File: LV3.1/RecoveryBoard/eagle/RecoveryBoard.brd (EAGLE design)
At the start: 120.9 x 54.6 mm, 92 parts, among them IC1 BD62120AEFJ-E2, Q1 BSS123, Q2 BSS123, Q3 BSS123, Q6 MOSFET-PCH-SOT23-6, U1 STM32F042K6, U10 TPS63070, Y1 ECS-160-10-36Q-ES-TR

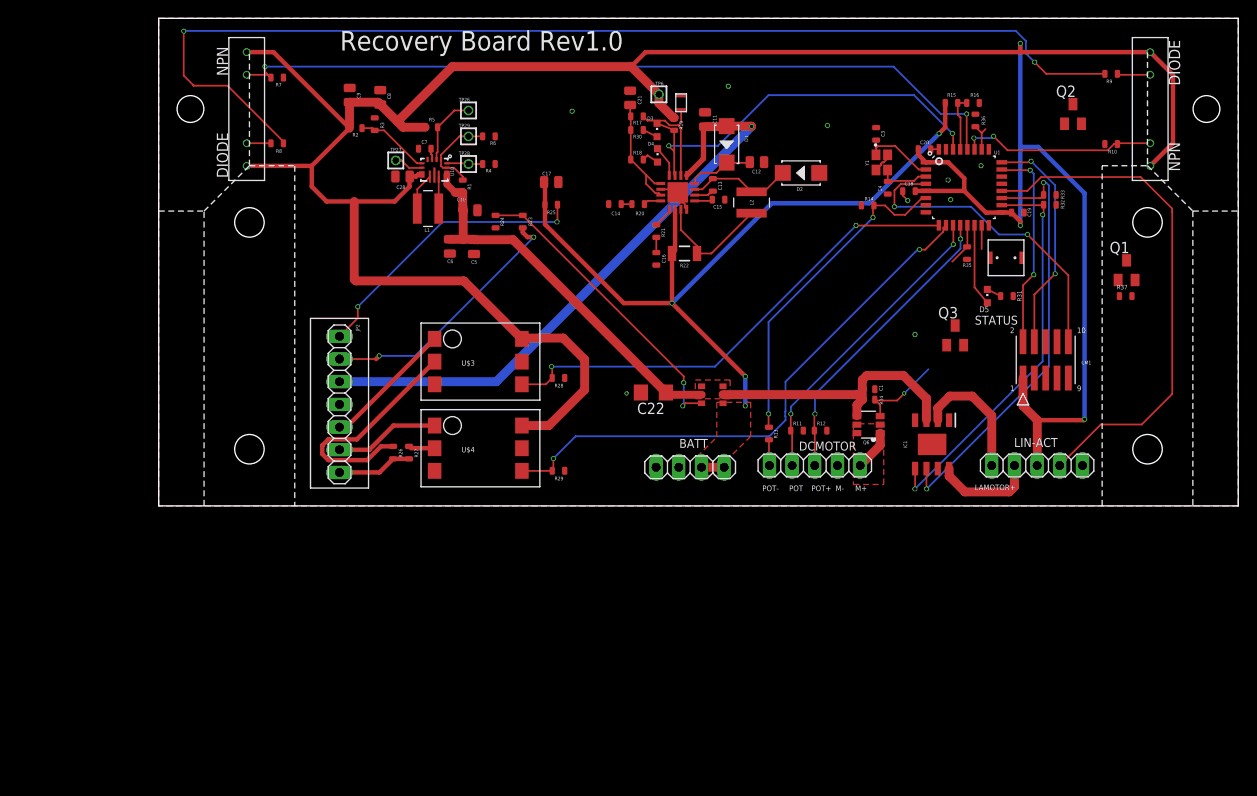
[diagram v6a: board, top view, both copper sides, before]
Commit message: edited board after design meeting on 1/15
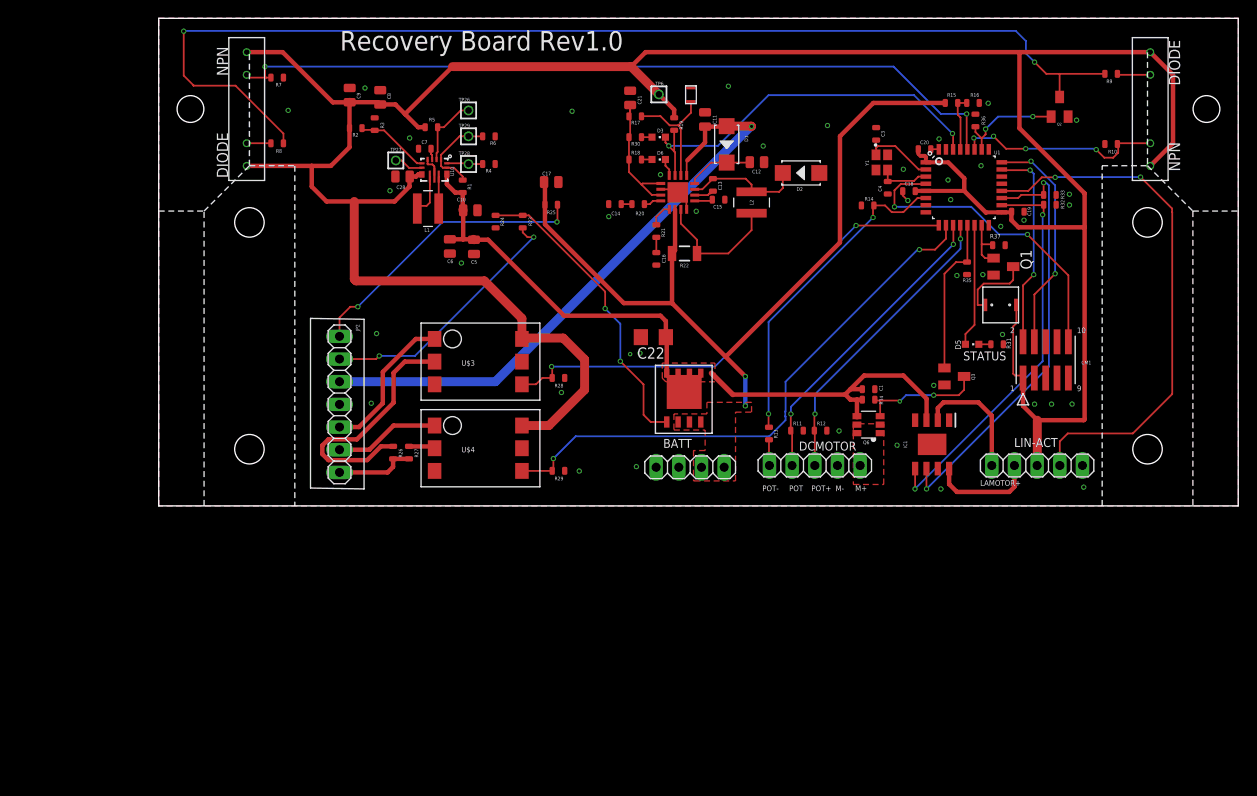
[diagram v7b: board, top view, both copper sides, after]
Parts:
- removed D4: (no value), led:CHIPLED_0603
- added D6: SML-D12U1WT86, led:CHIPLED_0603
- D3, D5: value (none) -> SML-D12U1WT86
- R26: value TBD -> 50
- R28: value 10k -> 50
- U$8: value AO6405 -> SI7465DP; device Q--AO6405--P-CH MOSFET for Arm Switch:AO6405 -> Q--Si7465DP--Vishay Power MOSFET with multple S+D leads:SI7465DP
- moved R37 15.3 mm to (94.1, 29.2)
- moved Q1 13.8 mm to (94.6, 26.8), turned to 270 degrees
- moved C22 6.20 mm to (55.4, 18.9)
- moved D5 5.66 mm to (91.1, 18.1), turned to 270 degrees
- moved U$8 5.59 mm to (56.9, 9.40), turned to 90 degrees
- moved R31 5.51 mm to (93.9, 18.1)
- moved U$7 5.31 mm to (94.3, 22.5), turned to 0 degrees
- moved Q3 4.60 mm to (89.1, 14.5), turned to 270 degrees
- moved Q2 1.70 mm to (100.9, 44.7)
- moved R35 1.70 mm to (90.5, 26.6)
- moved U$6 1.42 mm to (59.6, 46.0)
- moved R30 0.82 mm to (53.4, 41.3)
- moved D3 0.82 mm to (56.0, 41.3), turned to 270 degrees
- moved R17 0.20 mm to (53.4, 43.6)
- moved R18 0.20 mm to (53.4, 38.8)
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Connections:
- net N$15 renamed LED
- net N$8 renamed SPKR
- net +12V: now also U$8.D
- net ACOK: now also U$5.!ACOK; no longer U$5.~ACOK
- net GND: now also U$5.!EN; no longer U$5.~EN
- net N$13: now also D6.C, U$5.!CHGOK; no longer D4.C, U$5.~CHGOK
- net N$17: now also D6.A; no longer D4.A
- net VBAT: now also U$8.S1, U$8.S2, U$8.S3; no longer U$8.S
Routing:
- net DCM_ON: track 4.78 -> 17.8 mm
- net SENSOR_ON: track 3.45 -> 12.0 mm, vias 0 -> 2
- net N$1: track 0.00 -> 8.48 mm
- net 3.3V: track 312.5 -> 317.8 mm, vias 3 -> 0
- net LED: track 9.19 -> 13.8 mm
- net DCM+: track 4.55 -> 0.00 mm
- net N$6: track 9.45 -> 13.9 mm, vias 1 -> 2
- net SPKR: track 2.66 -> 6.06 mm
- net N$27: track 125.4 -> 128.5 mm
- net +12V: track 75.0 -> 77.3 mm
- net CHUTE: track 14.7 -> 16.8 mm
- net N$7: track 26.3 -> 28.2 mm
- net N$12: track 13.9 -> 15.7 mm
- net POT_OUT_AN: track 57.9 -> 59.4 mm, vias 0 -> 2
- net N$20: track 11.9 -> 13.5 mm
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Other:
- board text added: "TODO 1. I have CAN and USART Pins currenlty doing nothing 2. Need to add locking button 3. Update H-Bridge symbol"
- board text removed: "TODO 1. I have CAN and USART Pins currenlty doing nothing 2. Need to add locking button 3. Update Pin descriptions from schematic"

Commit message: adding new hbridge schematic
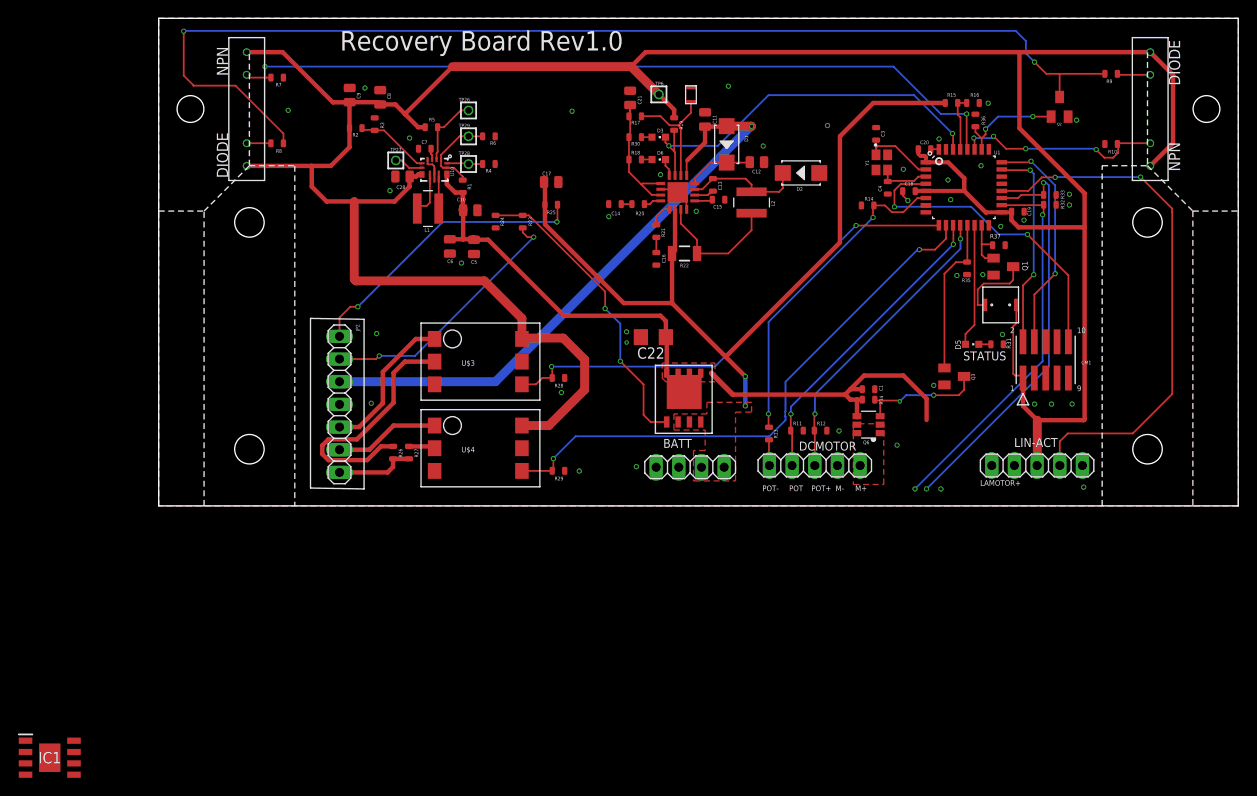
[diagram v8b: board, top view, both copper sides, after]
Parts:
- moved IC1 104.9 mm to (-12.2, -28.2), turned to 0 degrees
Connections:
- removed net LAMOTOR+: IC1.2, J2.1
- new net N$8: IC1.8, J2.2
- net GND: no longer IC1.7
- net LAMOTOR-: now also IC1.2, J2.1; no longer IC1.8, J2.2
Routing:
- net LAMOTOR+: track 13.9 -> 0.00 mm
- net LAMOTOR-: track 12.0 -> 0.00 mm
- net IN1: track 44.8 -> 42.5 mm
- net IN2: track 48.9 -> 46.6 mm
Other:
- board text removed: "is this dumb?"
